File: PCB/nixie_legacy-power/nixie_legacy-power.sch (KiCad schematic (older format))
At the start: 23 parts, among them J1 Barrel_Jack, J2 HEADER_3, Q1 BC547, Q2 MPSA56-AP, Q3 IRF740, U1 NE555P

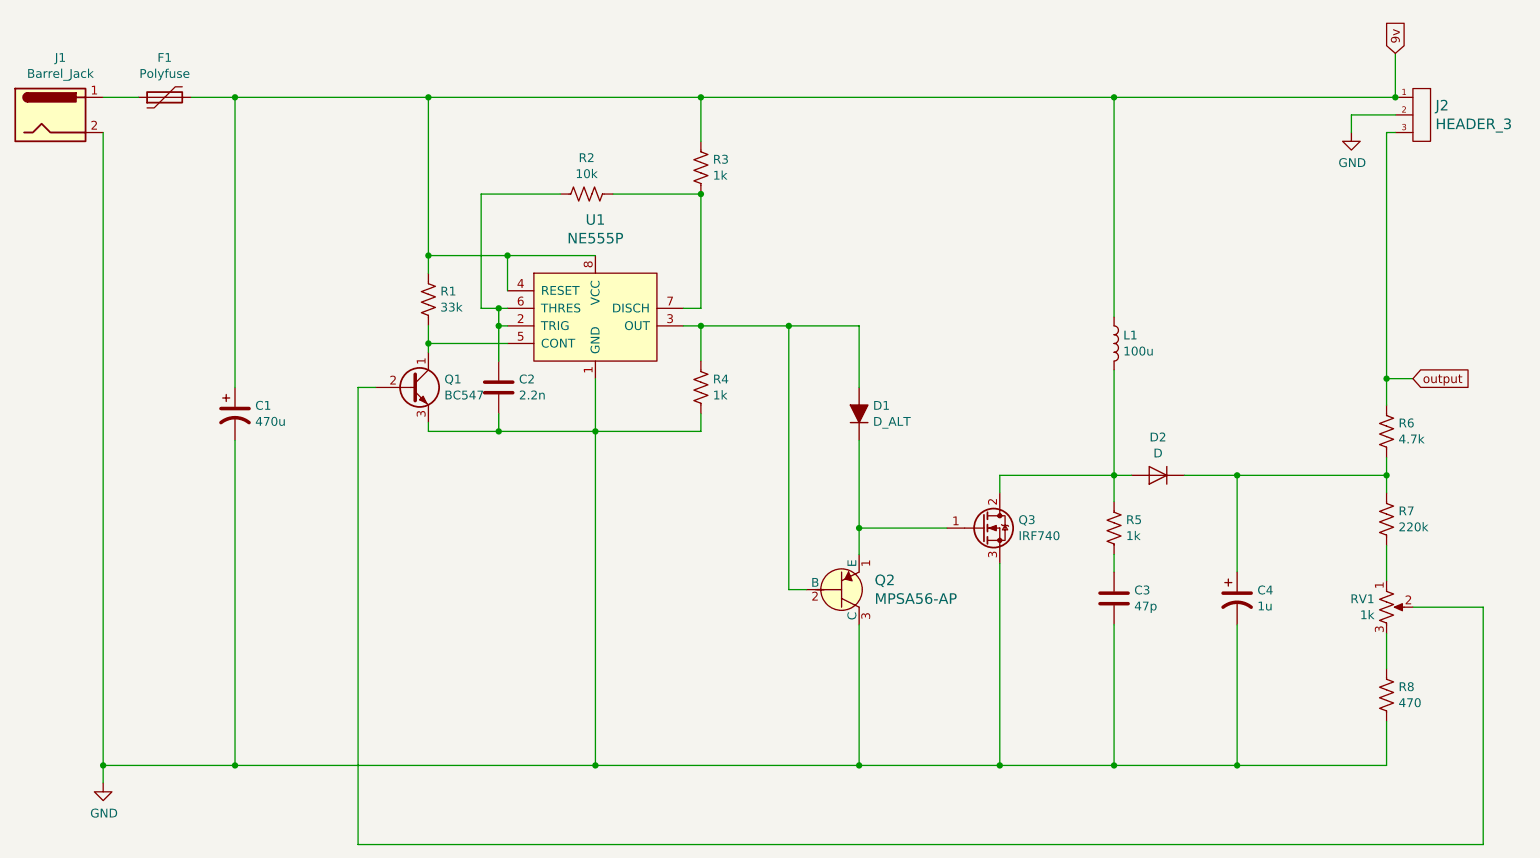
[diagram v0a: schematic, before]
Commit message: Updating power PCB to v2 to include 5v regulator and support post hole
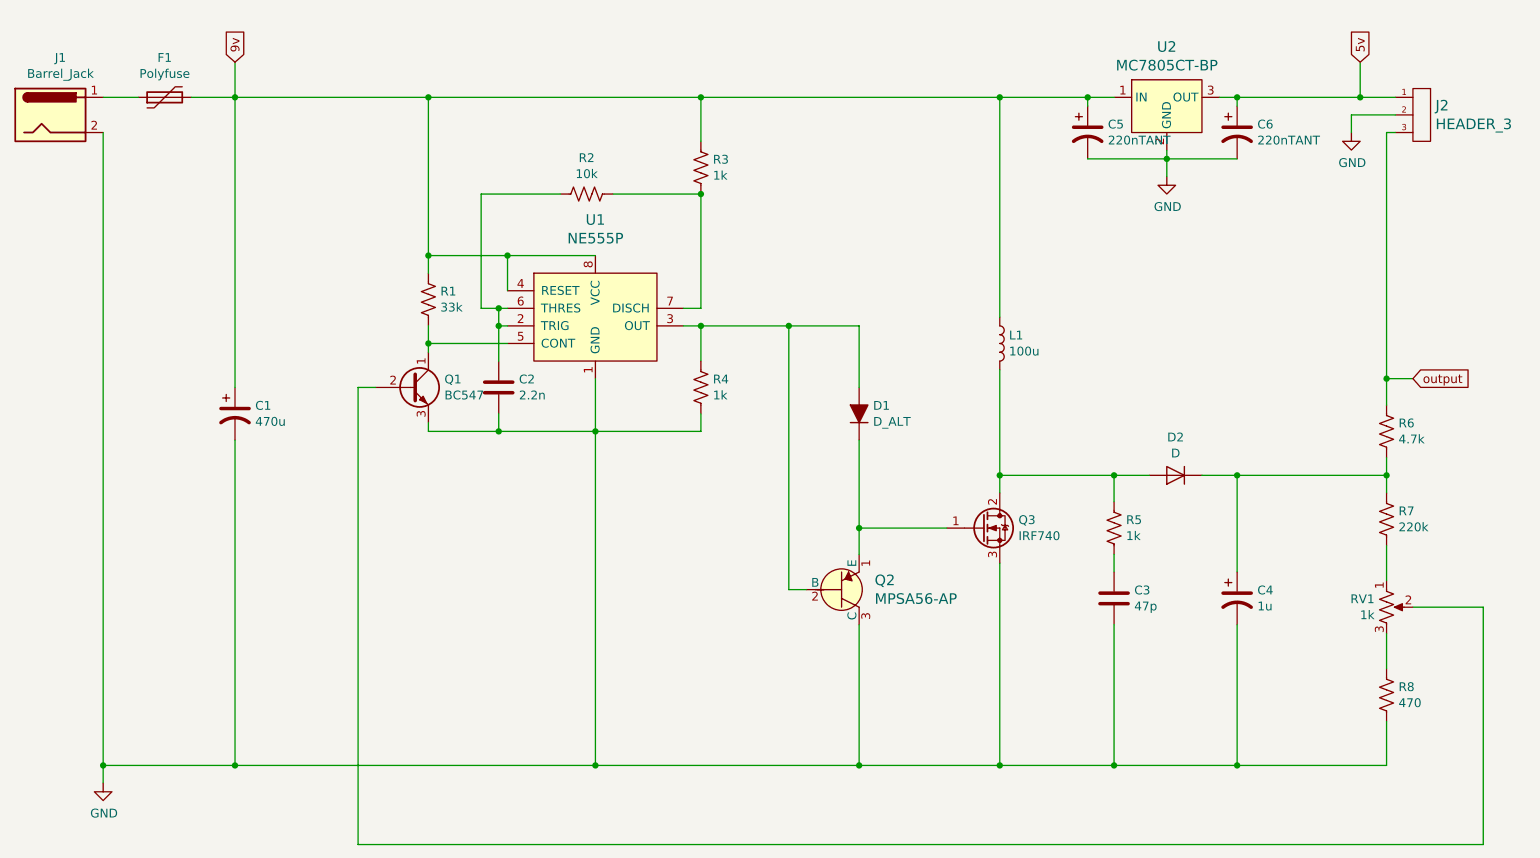
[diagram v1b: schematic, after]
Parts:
- added C5, C6: 220nTANT, Capacitor_THT:C_Disc_D3.8mm_W2.6mm_P2.50mm, symbol Device:CP1
- added U2: MC7805CT-BP, digikey-footprints:TO-220-3, symbol dk_PMIC-Voltage-Regulators-Linear:MC7805CT-BP
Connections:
- net 9v: now also C5.1, U2.1 (IN); no longer J2.1
- net GND: now also C5.2, C6.2, U2.2 (GND)
- new net 5v: C6.1, J2.1, U2.3 (OUT)
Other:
- moved on the sheet: D2, L1
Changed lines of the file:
@@
 EESchema Schematic File Version 4
+LIBS:nixie_legacy-power-cache
 EELAYER 29 0
 EELAYER END
@@
 L Device:L L1
 U 1 1 60FBEAA3
-P 7850 3100
-F 0 "L1" H 7902 3146 50  0000 L CNN
-F 1 "100u" H 7902 3055 50  0000 L CNN
-F 2 "Inductor_THT:L_Radial_D8.7mm_P5.00mm_Fastron_07HCP" H 7850 3100 50  0001 C CNN
-F 3 "~" H 7850 3100 50  0001 C CNN
-	1    7850 3100
+P 7200 3100
+F 0 "L1" H 7252 3146 50  0000 L CNN
+F 1 "100u" H 7252 3055 50  0000 L CNN
+F 2 "Inductor_THT:L_Radial_D8.7mm_P5.00mm_Fastron_07HCP" H 7200 3100 50  0001 C CNN
+F 3 "~" H 7200 3100 50  0001 C CNN
+	1    7200 3100
 	1    0    0    -1
 $EndComp
@@
 L Device:D D2
 U 1 1 60FC1717
-P 8100 3850
-F 0 "D2" H 8100 3634 50  0000 C CNN
-F 1 "D" H 8100 3725 50  0000 C CNN
-F 2 "Diode_THT:D_DO-41_SOD81_P7.62mm_Horizontal" H 8100 3850 50  0001 C CNN
-F 3 "~" H 8100 3850 50  0001 C CNN
-	1    8100 3850
+P 8200 3850
+F 0 "D2" H 8200 3634 50  0000 C CNN
+F 1 "D" H 8200 3725 50  0000 C CNN
+F 2 "Diode_THT:D_DO-41_SOD81_P7.62mm_Horizontal" H 8200 3850 50  0001 C CNN
+F 3 "~" H 8200 3850 50  0001 C CNN
+	1    8200 3850
 	-1   0    0    1
 $EndComp
@@
 	3950 2700 3950 2600
 Wire Wire Line
-	7950 3850 7850 3850
-Wire Wire Line
-	7850 3850 7850 4000
-Wire Wire Line
 	7850 4700 7850 5500
 Connection ~ 7850 5500
-Connection ~ 7850 3850
 Wire Wire Line
 	6400 3350 6400 3000
@@
 	8550 4400 8550 3850
 Wire Wire Line
-	8250 3850 8550 3850
+	8350 3850 8550 3850
 Wire Wire Line
 	8550 3850 9400 3850
@@
 Wire Wire Line
 	6900 4150 6400 4150
-Wire Wire Line
-	7200 3850 7850 3850
 $Comp
 L Transistor_FET:IRF740 Q3
@@
 Wire Wire Line
 	5500 3000 6000 3000
-Wire Wire Line
-	7850 3250 7850 3850
-Wire Wire Line
-	7200 3950 7200 3850
 Wire Wire Line
 	6400 3650 6400 4150
@@
 Wire Wire Line
 	9200 1800 9450 1800
-Connection ~ 9450 1700
-Wire Wire Line
-	9450 1450 9450 1700
-Text GLabel 9450 1450 1    50   Input ~ 0
+Text GLabel 2850 1500 1    50   Input ~ 0
 9v
 Wire Wire Line
@@
 Connection ~ 9400 3300
 Wire Wire Line
-	7850 2950 7850 1700
-Connection ~ 7850 1700
-Wire Wire Line
-	7850 1700 9450 1700
+	7200 2950 7200 1700
 Wire Wire Line
 	5500 1950 5500 1700
 Connection ~ 5500 1700
-Wire Wire Line
-	5500 1700 7850 1700
+$Comp
+L Device:CP1 C5
+U 1 1 6130CE3E
+P 7700 1900
+F 0 "C5" H 7815 1946 50  0000 L CNN
+F 1 "220nTANT" H 7815 1855 50  0000 L CNN
+F 2 "Capacitor_THT:C_Disc_D3.8mm_W2.6mm_P2.50mm" H 7700 1900 50  0001 C CNN
+F 3 "~" H 7700 1900 50  0001 C CNN
+	1    7700 1900
+	1    0    0    -1
+$EndComp
+$Comp
+L power:GND #PWR0103
+U 1 1 6130D90B
+P 8150 2150
+F 0 "#PWR0103" H 8150 1900 50  0001 C CNN
+F 1 "GND" H 8155 1977 50  0000 C CNN
+F 2 "" H 8150 2150 50  0001 C CNN
+F 3 "" H 8150 2150 50  0001 C CNN
+	1    8150 2150
+	1    0    0    -1
+$EndComp
+Wire Wire Line
+	2850 1500 2850 1700
+$Comp
+L Device:CP1 C6
+U 1 1 61314C3E
+P 8550 1900
+F 0 "C6" H 8665 1946 50  0000 L CNN
+F 1 "220nTANT" H 8665 1855 50  0000 L CNN
+F 2 "Capacitor_THT:C_Disc_D3.8mm_W2.6mm_P2.50mm" H 8550 1900 50  0001 C CNN
+F 3 "~" H 8550 1900 50  0001 C CNN
+	1    8550 1900
+	1    0    0    -1
+$EndComp
+Wire Wire Line
+	8550 2050 8150 2050
+Wire Wire Line
+	8150 2000 8150 2050
+Connection ~ 8150 2050
+Wire Wire Line
+	8150 2050 8150 2150
+Wire Wire Line
+	8150 2050 7700 2050
+Wire Wire Line
+	7850 1700 7700 1700
+Connection ~ 7200 1700
+Text GLabel 9250 1500 1    50   Input ~ 0
+5v
+Wire Wire Line
+	9250 1500 9250 1700
+Wire Wire Line
+	9250 1700 9450 1700
+$Comp
+L dk_PMIC-Voltage-Regulators-Linear:MC7805CT-BP U2
+U 1 1 6133B0B2
+P 8150 1700
+F 0 "U2" H 8150 1987 60  0000 C CNN
+F 1 "MC7805CT-BP" H 8150 1881 60  0000 C CNN
+F 2 "digikey-footprints:TO-220-3" H 8350 1900 60  0001 L CNN
+F 3 "http://www.mccsemi.com/up_pdf/MC7805CT(TO-220).pdf" H 8350 2000 60  0001 L CNN
+F 4 "MC7805CT-BPMS-ND" H 8350 2100 60  0001 L CNN "Digi-Key_PN"
+F 5 "MC7805CT-BP" H 8350 2200 60  0001 L CNN "MPN"
+F 6 "Integrated Circuits (ICs)" H 8350 2300 60  0001 L CNN "Category"
+F 7 "PMIC - Voltage Regulators - Linear" H 8350 2400 60  0001 L CNN "Family"
+F 8 "http://www.mccsemi.com/up_pdf/MC7805CT(TO-220).pdf" H 8350 2500 60  0001 L CNN "DK_Datasheet_Link"
+F 9 "/product-detail/en/micro-commercial-co/MC7805CT-BP/MC7805CT-BPMS-ND/804682" H 8350 2600 60  0001 L CNN "DK_Detail_Page"
+F 10 "IC REG LINEAR 5V 1.5A TO220" H 8350 2700 60  0001 L CNN "Description"
+F 11 "Micro Commercial Co" H 8350 2800 60  0001 L CNN "Manufacturer"
+F 12 "Active" H 8350 2900 60  0001 L CNN "Status"
+	1    8150 1700
+	1    0    0    -1
+$EndComp
+Wire Wire Line
+	7850 3850 7850 4000
+Wire Wire Line
+	7850 3850 8050 3850
+Wire Wire Line
+	7850 3850 7200 3850
+Wire Wire Line
+	7200 3250 7200 3850
+Connection ~ 7850 3850
+Connection ~ 7200 3850
+Wire Wire Line
+	7200 3850 7200 3950
+Wire Wire Line
+	8450 1700 8550 1700
+Wire Wire Line
+	7700 1750 7700 1700
+Connection ~ 7700 1700
+Wire Wire Line
+	7700 1700 7200 1700
+Wire Wire Line
+	8550 1750 8550 1700
+Connection ~ 8550 1700
+Wire Wire Line
+	8550 1700 9250 1700
+Wire Wire Line
+	5500 1700 7200 1700
+Connection ~ 9250 1700
 $EndSCHEMATC

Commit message: power pcb. added input polarity protection diode and rearranged board to fit accordingly. removed ground plane from high voltage zone. (recommit)
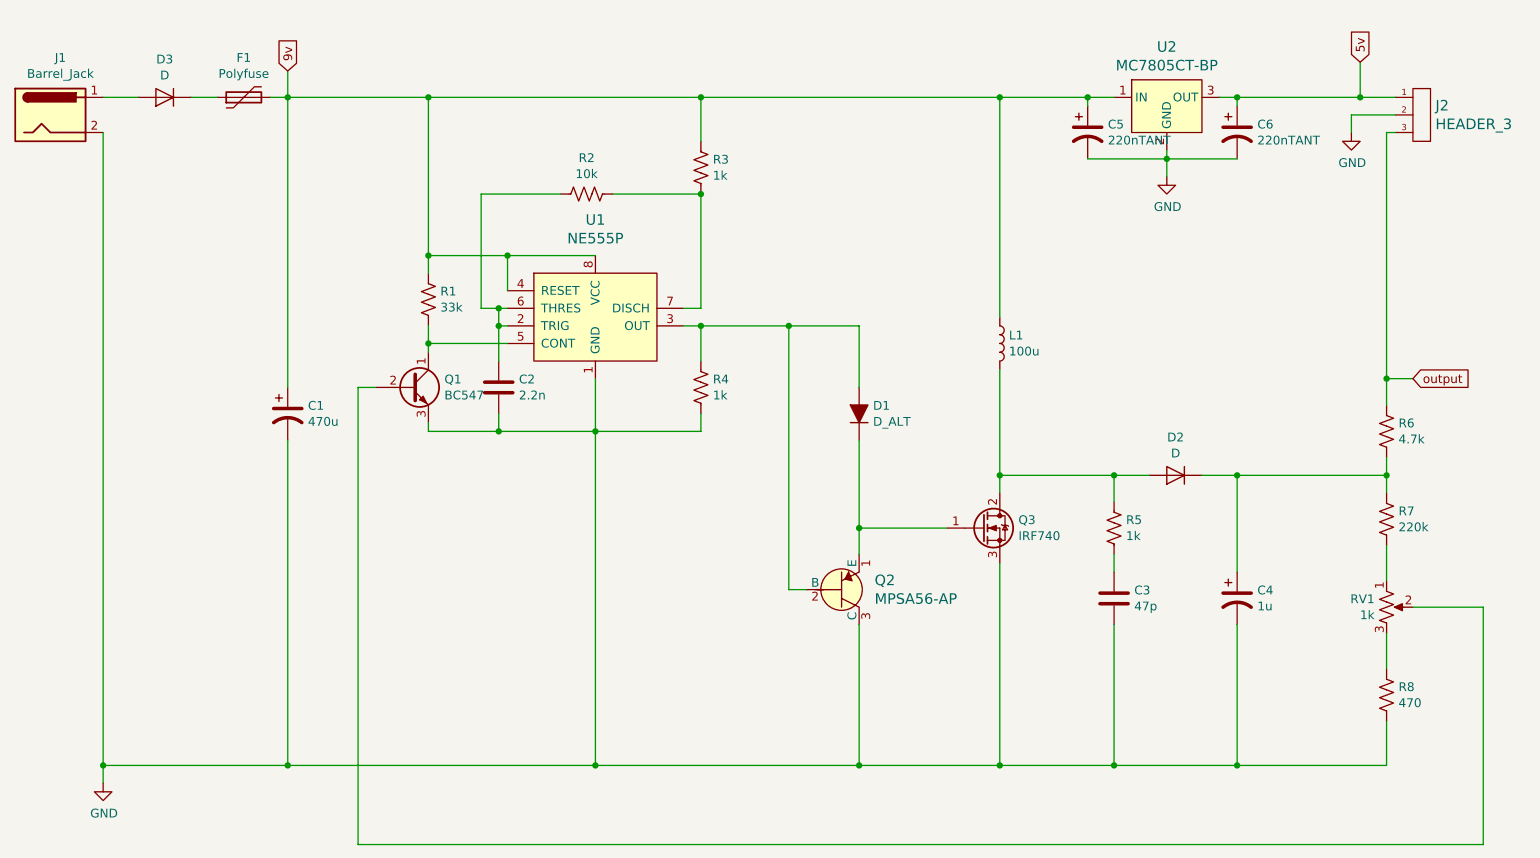
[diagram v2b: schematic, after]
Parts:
- added D3: D, Diode_THT:D_DO-41_SOD81_P2.54mm_Vertical_KathodeUp, symbol Device:D
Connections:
- net at F1.1: now also D3.1 (K); no longer J1.1
- new net: D3.2 (A), J1.1
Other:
- moved on the sheet: C1, F1
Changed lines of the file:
@@
 L Device:CP1 C1
 U 1 1 60FBB5AF
-P 2850 3500
-F 0 "C1" H 2965 3546 50  0000 L CNN
-F 1 "470u" H 2965 3455 50  0000 L CNN
-F 2 "Capacitor_THT:CP_Radial_D10.0mm_P5.00mm" H 2850 3500 50  0001 C CNN
-F 3 "~" H 2850 3500 50  0001 C CNN
-	1    2850 3500
+P 3150 3500
+F 0 "C1" H 3265 3546 50  0000 L CNN
+F 1 "470u" H 3265 3455 50  0000 L CNN
+F 2 "Capacitor_THT:CP_Radial_D10.0mm_P5.00mm" H 3150 3500 50  0001 C CNN
+F 3 "~" H 3150 3500 50  0001 C CNN
+	1    3150 3500
 	1    0    0    -1
 $EndComp
@@
 	5500 3000 5500 3200
 Wire Wire Line
-	2850 5500 2850 3650
+	3150 5500 3150 3650
 Wire Wire Line
 	4900 3600 4900 5500
@@
 	9400 4250 9400 4450
 Wire Wire Line
-	2100 5500 2850 5500
-Connection ~ 2850 5500
-Wire Wire Line
-	2850 5500 4900 5500
+	2100 5500 3150 5500
+Connection ~ 3150 5500
+Wire Wire Line
+	3150 5500 4900 5500
 Wire Wire Line
 	4900 5500 6400 5500
@@
 L Device:Polyfuse F1
 U 1 1 60FB616D
-P 2450 1700
-F 0 "F1" V 2675 1700 50  0000 C CNN
-F 1 "Polyfuse" V 2584 1700 50  0000 C CNN
-F 2 "Fuse:Fuse_Bourns_MF-RG300" H 2500 1500 50  0001 L CNN
-F 3 "~" H 2450 1700 50  0001 C CNN
-	1    2450 1700
+P 2900 1700
+F 0 "F1" V 3125 1700 50  0000 C CNN
+F 1 "Polyfuse" V 3034 1700 50  0000 C CNN
+F 2 "Fuse:Fuse_Bourns_MF-RG300" H 2950 1500 50  0001 L CNN
+F 3 "~" H 2900 1700 50  0001 C CNN
+	1    2900 1700
 	0    -1   -1   0
 $EndComp
@@
 Wire Wire Line
 	9200 1800 9450 1800
-Text GLabel 2850 1500 1    50   Input ~ 0
+Text GLabel 3150 1550 1    50   Input ~ 0
 9v
 Wire Wire Line
-	2600 1700 2850 1700
+	3050 1700 3150 1700
 Wire Wire Line
 	2100 1900 2100 5500
@@
 	3950 1700 5500 1700
 Wire Wire Line
-	2850 3350 2850 1700
-Connection ~ 2850 1700
-Wire Wire Line
-	2850 1700 3950 1700
+	3150 3350 3150 1700
+Connection ~ 3150 1700
+Wire Wire Line
+	3150 1700 3950 1700
 Wire Wire Line
 	9400 3300 9400 1900
@@
 $EndComp
 Wire Wire Line
-	2850 1500 2850 1700
+	3150 1550 3150 1700
 $Comp
 L Device:CP1 C6
@@
 	5500 1700 7200 1700
 Connection ~ 9250 1700
+Wire Wire Line
+	2600 1700 2750 1700
+$Comp
+L Device:D D3
+U 1 1 6114F2C2
+P 2450 1700
+F 0 "D3" H 2450 1484 50  0000 C CNN
+F 1 "D" H 2450 1575 50  0000 C CNN
+F 2 "Diode_THT:D_DO-41_SOD81_P2.54mm_Vertical_KathodeUp" H 2450 1700 50  0001 C CNN
+F 3 "~" H 2450 1700 50  0001 C CNN
+	1    2450 1700
+	-1   0    0    1
+$EndComp
 $EndSCHEMATC

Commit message: -power board: updated 7805 footprint to better fit piece, "A55" instead of "A56", 9v input pad shape swap so that ground makes sense -digit board: added resistor value, vertical connector, correct pinout for rear mounting to match header population on demux board -new_rtc_pcbHack: deprecated. works with v1 of digit boards (with bad header pinout) but no longer needed. did not update with time demux, only displayed idle animation and set menu
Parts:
- Q2: value MPSA56-AP -> MPSA55-AP
- U2: footprint digikey-footprints:TO-220-3 -> Package_TO_SOT_THT:TO-220-3_Vertical
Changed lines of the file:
@@
 P 6300 4500
 F 0 "Q2" H 6488 4553 60  0000 L CNN
-F 1 "MPSA56-AP" H 6488 4447 60  0000 L CNN
+F 1 "MPSA55-AP" H 6488 4447 60  0000 L CNN
 F 2 "digikey-footprints:TO-92-3_Formed_Leads" H 6500 4700 60  0001 L CNN
 F 3 "http://www.mccsemi.com/up_pdf/MPSA55-MPSA56(TO-92).pdf" H 6500 4800 60  0001 L CNN
@@
 F 0 "U2" H 8150 1987 60  0000 C CNN
 F 1 "MC7805CT-BP" H 8150 1881 60  0000 C CNN
-F 2 "digikey-footprints:TO-220-3" H 8350 1900 60  0001 L CNN
+F 2 "Package_TO_SOT_THT:TO-220-3_Vertical" H 8350 1900 60  0001 L CNN
 F 3 "http://www.mccsemi.com/up_pdf/MC7805CT(TO-220).pdf" H 8350 2000 60  0001 L CNN
 F 4 "MC7805CT-BPMS-ND" H 8350 2100 60  0001 L CNN "Digi-Key_PN"
